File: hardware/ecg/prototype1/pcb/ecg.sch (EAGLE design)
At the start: 21 parts

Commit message: no comment
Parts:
- removed C5: 10uF, adafruit:C-USC0805
- removed LED3: (no value), adafruit:LED3MM
- removed R3: (no value), resistor:R-EU_R0805
- added C6, C7: 1uF, adafruit:C-USC0805
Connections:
- removed net N$28: C3.2, U$1.DGND
- removed net N$31: LED3.A, R3.1
- new net N$27: C6.1, U$1.VCAP1
- new net N$32: C7.1, U$1.VCAP2
- new net ULED1: R1.2, U$1.GPIO1
- new net ULED2: R2.2, U$2.PIO0_7
- net GND: now also C3.2, C6.2, C7.2, U$1.DGND; no longer C5.2, LED3.C
- net VDD: now also JP5.1; no longer C5.1
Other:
- moved on the sheet: JP5, LED1, LED2, R1, R2, U$5
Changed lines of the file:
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@@
 <part name="GND5" library="supply1" deviceset="GND" device=""/>
 <part name="VDD3" library="supply1" deviceset="VDD" device=""/>
-<part name="C5" library="adafruit" deviceset="C-US" device="C0805" value="10uF"/>
 <part name="JP5" library="pinhead" deviceset="PINHD-1X2" device=""/>
 <part name="LED1" library="adafruit" deviceset="LED" device="3MM"/>
 <part name="LED2" library="adafruit" deviceset="LED" device="3MM"/>
-<part name="LED3" library="adafruit" deviceset="LED" device="3MM"/>
 <part name="R1" library="resistor" deviceset="R-EU_" device="R0805"/>
 <part name="R2" library="resistor" deviceset="R-EU_" device="R0805"/>
-<part name="R3" library="resistor" deviceset="R-EU_" device="R0805"/>
-<part name="GND8" library="supply1" deviceset="GND" device=""/>
 <part name="GND9" library="supply1" deviceset="GND" device=""/>
 <part name="GND10" library="supply1" deviceset="GND" device=""/>
+<part name="C6" library="adafruit" deviceset="C-US" device="C0805" value="1uF"/>
+<part name="GND11" library="supply1" deviceset="GND" device=""/>
+<part name="C7" library="adafruit" deviceset="C-US" device="C0805" value="1uF"/>
+<part name="GND12" library="supply1" deviceset="GND" device=""/>
+<part name="GND13" library="supply1" deviceset="GND" device=""/>
 </parts>
 <sheets>
@@
 <instance part="GND6" gate="1" x="121.92" y="104.14" rot="R180"/>
 <instance part="VDD5" gate="G$1" x="116.84" y="106.68"/>
-<instance part="U$5" gate="G$1" x="-7.62" y="114.3"/>
-<instance part="VDD6" gate="G$1" x="-17.78" y="124.46"/>
-<instance part="GND7" gate="1" x="-2.54" y="109.22"/>
+<instance part="U$5" gate="G$1" x="-5.08" y="104.14"/>
+<instance part="VDD6" gate="G$1" x="-15.24" y="114.3"/>
+<instance part="GND7" gate="1" x="0" y="99.06"/>
 <instance part="JP2" gate="A" x="132.08" y="93.98"/>
 <instance part="JP3" gate="A" x="-48.26" y="76.2"/>
@@
 <instance part="GND5" gate="1" x="114.3" y="71.12" rot="R180"/>
 <instance part="VDD3" gate="G$1" x="106.68" y="63.5" rot="R180"/>
-<instance part="C5" gate="G$1" x="83.82" y="124.46" rot="R270"/>
-<instance part="JP5" gate="G$1" x="12.7" y="119.38"/>
-<instance part="LED1" gate="G$1" x="-66.04" y="124.46"/>
-<instance part="LED2" gate="G$1" x="-55.88" y="124.46"/>
-<instance part="LED3" gate="G$1" x="-45.72" y="124.46"/>
-<instance part="R1" gate="G$1" x="-66.04" y="132.08" rot="R90"/>
-<instance part="R2" gate="G$1" x="-55.88" y="132.08" rot="R90"/>
-<instance part="R3" gate="G$1" x="-45.72" y="132.08" rot="R90"/>
-<instance part="GND8" gate="1" x="-45.72" y="116.84"/>
-<instance part="GND9" gate="1" x="-55.88" y="116.84"/>
-<instance part="GND10" gate="1" x="-66.04" y="116.84"/>
+<instance part="JP5" gate="G$1" x="15.24" y="109.22"/>
+<instance part="LED1" gate="G$1" x="-50.8" y="99.06"/>
+<instance part="LED2" gate="G$1" x="-40.64" y="99.06"/>
+<instance part="R1" gate="G$1" x="-50.8" y="106.68" rot="R90"/>
+<instance part="R2" gate="G$1" x="-40.64" y="106.68" rot="R90"/>
+<instance part="GND9" gate="1" x="-40.64" y="91.44"/>
+<instance part="GND10" gate="1" x="-50.8" y="91.44"/>
+<instance part="C6" gate="G$1" x="38.1" y="53.34" rot="R90"/>
+<instance part="GND11" gate="1" x="45.72" y="53.34" rot="R90"/>
+<instance part="C7" gate="G$1" x="-43.18" y="53.34" rot="R270"/>
+<instance part="GND12" gate="1" x="-50.8" y="53.34" rot="R270"/>
+<instance part="GND13" gate="1" x="38.1" y="86.36" rot="R90"/>
 </instances>
 <busses>
@@
 <pinref part="U$3" gate="G$1" pin="VSS"/>
 <pinref part="GND2" gate="1" pin="GND"/>
-<pinref part="C5" gate="G$1" pin="2"/>
-<wire x1="78.74" y1="124.46" x2="66.04" y2="124.46" width="0.1524" layer="91"/>
-<wire x1="66.04" y1="124.46" x2="66.04" y2="99.06" width="0.1524" layer="91"/>
-<wire x1="66.04" y1="99.06" x2="71.12" y2="99.06" width="0.1524" layer="91"/>
-<junction x="71.12" y="99.06"/>
 </segment>
 <segment>
@@
 <pinref part="GND7" gate="1" pin="GND"/>
 <pinref part="JP5" gate="G$1" pin="2"/>
-<wire x1="0" y1="119.38" x2="10.16" y2="119.38" width="0.1524" layer="91"/>
-<wire x1="0" y1="119.38" x2="0" y2="111.76" width="0.1524" layer="91"/>
-<wire x1="0" y1="111.76" x2="-2.54" y2="111.76" width="0.1524" layer="91"/>
-<junction x="-2.54" y="111.76"/>
+<wire x1="2.54" y1="109.22" x2="12.7" y2="109.22" width="0.1524" layer="91"/>
+<wire x1="2.54" y1="109.22" x2="2.54" y2="101.6" width="0.1524" layer="91"/>
+<wire x1="2.54" y1="101.6" x2="0" y2="101.6" width="0.1524" layer="91"/>
+<junction x="0" y="101.6"/>
 </segment>
 <segment>
@@
 </segment>
 <segment>
-<pinref part="LED3" gate="G$1" pin="C"/>
-<pinref part="GND8" gate="1" pin="GND"/>
-</segment>
-<segment>
 <pinref part="LED2" gate="G$1" pin="C"/>
 <pinref part="GND9" gate="1" pin="GND"/>
@@
 <pinref part="LED1" gate="G$1" pin="C"/>
 <pinref part="GND10" gate="1" pin="GND"/>
+</segment>
+<segment>
+<pinref part="C6" gate="G$1" pin="2"/>
+<pinref part="GND11" gate="1" pin="GND"/>
+</segment>
+<segment>
+<pinref part="C7" gate="G$1" pin="2"/>
+<pinref part="GND12" gate="1" pin="GND"/>
+</segment>
+<segment>
+<pinref part="C3" gate="G$1" pin="2"/>
+<wire x1="33.02" y1="86.36" x2="35.56" y2="86.36" width="0.1524" layer="91"/>
+<wire x1="35.56" y1="86.36" x2="35.56" y2="83.82" width="0.1524" layer="91"/>
+<pinref part="U$1" gate="G$1" pin="DGND"/>
+<wire x1="35.56" y1="83.82" x2="20.32" y2="83.82" width="0.1524" layer="91"/>
+<pinref part="GND13" gate="1" pin="GND"/>
+<junction x="35.56" y="86.36"/>
 </segment>
 </net>
@@
 <pinref part="VDD2" gate="G$1" pin="VDD"/>
 <wire x1="101.6" y1="114.3" x2="96.52" y2="114.3" width="0.1524" layer="91"/>
-<pinref part="C5" gate="G$1" pin="1"/>
-<wire x1="86.36" y1="124.46" x2="96.52" y2="124.46" width="0.1524" layer="91"/>
-<wire x1="96.52" y1="124.46" x2="96.52" y2="114.3" width="0.1524" layer="91"/>
-<junction x="96.52" y="114.3"/>
 </segment>
 <segment>
@@
 <segment>
 <pinref part="VDD6" gate="G$1" pin="VDD"/>
-<wire x1="-17.78" y1="121.92" x2="-17.78" y2="114.3" width="0.1524" layer="91"/>
+<wire x1="-15.24" y1="111.76" x2="-15.24" y2="104.14" width="0.1524" layer="91"/>
 <pinref part="U$5" gate="G$1" pin="-"/>
-<wire x1="-17.78" y1="114.3" x2="-12.7" y2="114.3" width="0.1524" layer="91"/>
-<wire x1="-12.7" y1="114.3" x2="-12.7" y2="121.92" width="0.1524" layer="91"/>
-<junction x="-12.7" y="114.3"/>
-<wire x1="-12.7" y1="121.92" x2="10.16" y2="121.92" width="0.1524" layer="91"/>
+<wire x1="-15.24" y1="104.14" x2="-10.16" y2="104.14" width="0.1524" layer="91"/>
+<wire x1="-10.16" y1="104.14" x2="-10.16" y2="111.76" width="0.1524" layer="91"/>
+<junction x="-10.16" y="104.14"/>
+<wire x1="-10.16" y1="111.76" x2="12.7" y2="111.76" width="0.1524" layer="91"/>
+<pinref part="JP5" gate="G$1" pin="1"/>
 </segment>
 </net>
@@
 </segment>
 </net>
-<net name="N$28" class="0">
-<segment>
-<pinref part="C3" gate="G$1" pin="2"/>
-<wire x1="33.02" y1="86.36" x2="35.56" y2="86.36" width="0.1524" layer="91"/>
-<wire x1="35.56" y1="86.36" x2="35.56" y2="83.82" width="0.1524" layer="91"/>
-<pinref part="U$1" gate="G$1" pin="DGND"/>
-<wire x1="35.56" y1="83.82" x2="20.32" y2="83.82" width="0.1524" layer="91"/>
-</segment>
-</net>
 <net name="N$29" class="0">
 <segment>
@@
 </segment>
 </net>
-<net name="N$31" class="0">
-<segment>
-<pinref part="LED3" gate="G$1" pin="A"/>
-<pinref part="R3" gate="G$1" pin="1"/>
-</segment>
-</net>
+<net name="ULED1" class="0">
+<segment>
+<pinref part="U$1" gate="G$1" pin="GPIO1"/>
+<wire x1="-20.32" y1="50.8" x2="-25.4" y2="50.8" width="0.1524" layer="91"/>
+<label x="-25.4" y="50.8" size="1.778" layer="95" rot="R180" xref="yes"/>
+</segment>
+<segment>
+<pinref part="R1" gate="G$1" pin="2"/>
+<wire x1="-50.8" y1="111.76" x2="-50.8" y2="114.3" width="0.1524" layer="91"/>
+<label x="-50.8" y="114.3" size="1.778" layer="95" rot="R90" xref="yes"/>
+</segment>
+</net>
+<net name="N$27" class="0">
+<segment>
+<pinref part="U$1" gate="G$1" pin="VCAP1"/>
+<pinref part="C6" gate="G$1" pin="1"/>
+<wire x1="20.32" y1="53.34" x2="35.56" y2="53.34" width="0.1524" layer="91"/>
+</segment>
+</net>
+<net name="N$32" class="0">
+<segment>
+<pinref part="C7" gate="G$1" pin="1"/>
+<pinref part="U$1" gate="G$1" pin="VCAP2"/>
+<wire x1="-40.64" y1="53.34" x2="-20.32" y2="53.34" width="0.1524" layer="91"/>
+</segment>
+</net>
+<net name="ULED2" class="0">
+<segment>
+<pinref part="U$2" gate="G$1" pin="PIO0_7"/>
+<wire x1="104.14" y1="83.82" x2="114.3" y2="83.82" width="0.1524" layer="91"/>
+<label x="114.3" y="83.82" size="1.778" layer="95" xref="yes"/>
+</segment>
+<segment>
+<pinref part="R2" gate="G$1" pin="2"/>
+<wire x1="-40.64" y1="111.76" x2="-40.64" y2="114.3" width="0.1524" layer="91"/>
+<label x="-40.64" y="114.3" size="1.778" layer="95" rot="R90" xref="yes"/>
+</segment>
+</net>

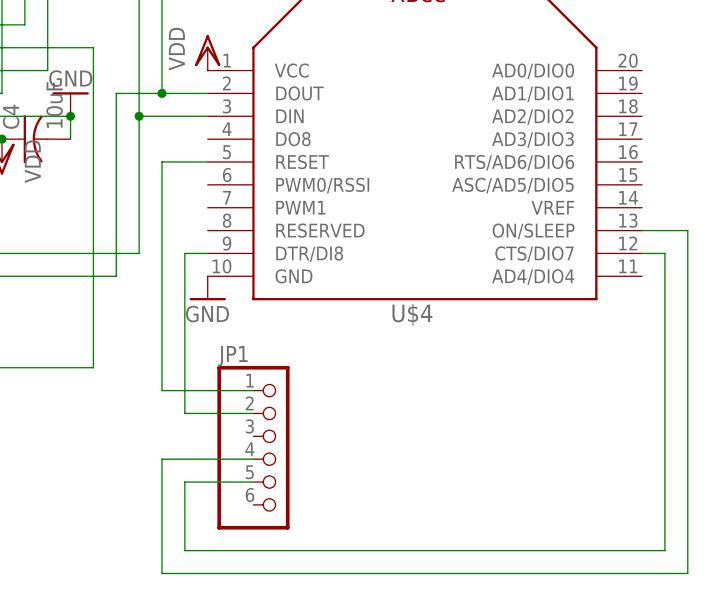
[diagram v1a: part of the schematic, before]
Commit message: PCB v0.1.2, sent to EuroCircuits for fab.
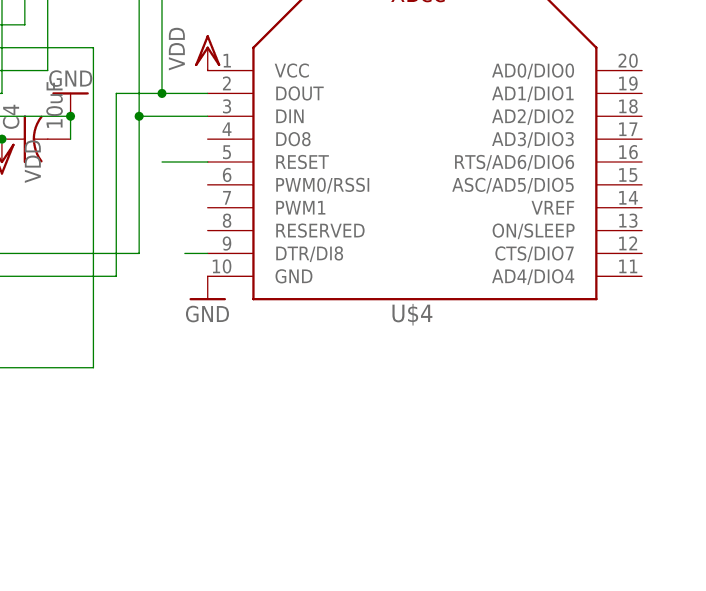
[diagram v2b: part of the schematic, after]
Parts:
- removed JP1: (no value), pinhead:PINHD-1X6
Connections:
- removed net N$18: JP1.1, U$4.RESET
- removed net N$19: JP1.2, U$4.DTR/DI8
- removed net N$25: JP1.4, U$4.ON/SLEEP
- removed net N$26: JP1.5, U$4.CTS/DIO7
- new net N$28: U$4.RESET
- new net N$31: U$4.DTR/DI8
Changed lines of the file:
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@@
 <part name="JP2" library="pinhead" deviceset="PINHD-1X6" device=""/>
 <part name="JP3" library="pinhead" deviceset="PINHD-2X5" device=""/>
-<part name="JP1" library="pinhead" deviceset="PINHD-1X6" device=""/>
 <part name="VDD1" library="supply1" deviceset="VDD" device=""/>
 <part name="GND3" library="supply1" deviceset="GND" device=""/>
@@
 <instance part="JP2" gate="A" x="132.08" y="93.98"/>
 <instance part="JP3" gate="A" x="-48.26" y="76.2"/>
-<instance part="JP1" gate="A" x="137.16" y="30.48"/>
 <instance part="VDD1" gate="G$1" x="25.4" y="96.52"/>
 <instance part="GND3" gate="1" x="30.48" y="48.26" rot="R90"/>
@@
 </segment>
 </net>
-<net name="N$18" class="0">
-<segment>
-<pinref part="U$4" gate="G$1" pin="RESET"/>
-<wire x1="129.54" y1="63.5" x2="124.46" y2="63.5" width="0.1524" layer="91"/>
-<wire x1="124.46" y1="63.5" x2="124.46" y2="38.1" width="0.1524" layer="91"/>
-<pinref part="JP1" gate="A" pin="1"/>
-<wire x1="124.46" y1="38.1" x2="134.62" y2="38.1" width="0.1524" layer="91"/>
-</segment>
-</net>
-<net name="N$19" class="0">
-<segment>
-<pinref part="U$4" gate="G$1" pin="DTR/DI8"/>
-<wire x1="129.54" y1="53.34" x2="127" y2="53.34" width="0.1524" layer="91"/>
-<wire x1="127" y1="53.34" x2="127" y2="35.56" width="0.1524" layer="91"/>
-<pinref part="JP1" gate="A" pin="2"/>
-<wire x1="127" y1="35.56" x2="134.62" y2="35.56" width="0.1524" layer="91"/>
-</segment>
-</net>
-<net name="N$25" class="0">
-<segment>
-<pinref part="U$4" gate="G$1" pin="ON/SLEEP"/>
-<wire x1="177.8" y1="55.88" x2="182.88" y2="55.88" width="0.1524" layer="91"/>
-<wire x1="182.88" y1="55.88" x2="182.88" y2="17.78" width="0.1524" layer="91"/>
-<wire x1="182.88" y1="17.78" x2="124.46" y2="17.78" width="0.1524" layer="91"/>
-<wire x1="124.46" y1="17.78" x2="124.46" y2="30.48" width="0.1524" layer="91"/>
-<pinref part="JP1" gate="A" pin="4"/>
-<wire x1="124.46" y1="30.48" x2="134.62" y2="30.48" width="0.1524" layer="91"/>
-</segment>
-</net>
-<net name="N$26" class="0">
-<segment>
-<pinref part="U$4" gate="G$1" pin="CTS/DIO7"/>
-<wire x1="177.8" y1="53.34" x2="180.34" y2="53.34" width="0.1524" layer="91"/>
-<wire x1="180.34" y1="53.34" x2="180.34" y2="20.32" width="0.1524" layer="91"/>
-<wire x1="180.34" y1="20.32" x2="127" y2="20.32" width="0.1524" layer="91"/>
-<wire x1="127" y1="20.32" x2="127" y2="27.94" width="0.1524" layer="91"/>
-<pinref part="JP1" gate="A" pin="5"/>
-<wire x1="127" y1="27.94" x2="134.62" y2="27.94" width="0.1524" layer="91"/>
-</segment>
-</net>
 <net name="N$29" class="0">
 <segment>
@@
 </segment>
 </net>
+<net name="N$28" class="0">
+<segment>
+<pinref part="U$4" gate="G$1" pin="RESET"/>
+<wire x1="129.54" y1="63.5" x2="124.46" y2="63.5" width="0.1524" layer="91"/>
+</segment>
+</net>
+<net name="N$31" class="0">
+<segment>
+<pinref part="U$4" gate="G$1" pin="DTR/DI8"/>
+<wire x1="129.54" y1="53.34" x2="127" y2="53.34" width="0.1524" layer="91"/>
+</segment>
+</net>
